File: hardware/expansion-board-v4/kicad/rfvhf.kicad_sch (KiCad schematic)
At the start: 19 parts, among them J10 U.FL_VHF(经尾线转SMA), U21 BK4819QN32SC, U22 PCM1808PWR, Y4 26MHz TCXO <=2.5ppm

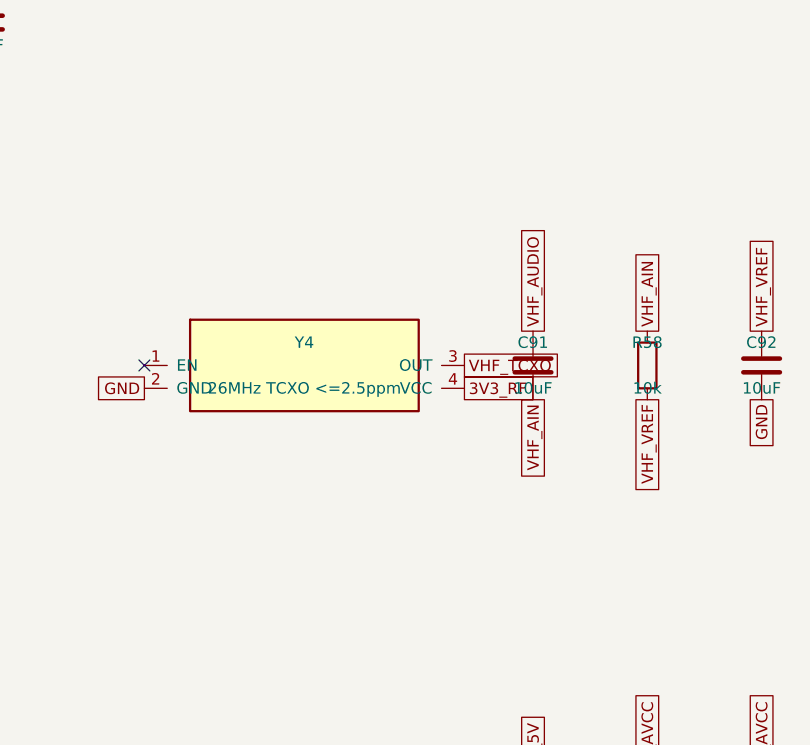
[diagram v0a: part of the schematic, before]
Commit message: v4.7: SW3 主电源键接 /QON + TCXO 输出隔直 + 覆铜填充参数固化
**SW3 主电源键**。电池在位时 SYS 恒供电，整板此前没有任何机械总电门：
微雪 Key3 只关得掉载板自己，而整机 5V 是扩展板升压产的；J1 的 40 脚里
没有一根电源控制线。唯一出路是 SY6970 的 BATFET——所以引 U19.12(/QON)
到板边的 TS24CA 侧按键（按住 1.25~2.25s 开机，BUS 拔掉时按 12~18s 硬复位），
不依赖固件。摆在 USB 口同侧贴板边 (97.882, 39.103)，R7/R8 那组往板内让 4mm 腾位。

封装按规格书 1:1：电气端子 1.2×0.6 中心距 3.4、固定脚 1.3×1.05 外缘跨度 5.3、
两个 φ0.55 定位孔在 X+0.70。两个坑记在封装 descr 里：①定位孔的 layers 必须写
「*.Cu」而不是「F&B.Cu」，否则 6 层板的内层覆铜照样压上来（每孔 5 条
hole_clearance、实际间距 0）；②孔心不能按「上下排焊盘空档的中心」推，那样
错 0.75mm、柱子插不进去。

**TCXO 输出隔直**。Epson brief sheet 的输出负载条件栏写死 DC cut = 0.01µF，
原设计 Y4.3 直连 BK4819 的 XI。补 C99(0402 100pF C0G) 串联 + R61(0402 10k)
负载，VHF_TCXO 拆成 VHF_TCXO_OUT / VHF_TCXO 两网。这里只能用 0402：两焊盘
净空 2.28mm，0603 含焊盘约 2.8mm 放不下，而 Y4 四周被 C76/C98/U21 夹死挪不开。
Y4 符号 pin1 由 EN 改 NC（选型库 fcfYN=N，无压控，悬空正确）。

**覆铜填充参数固化**（本次真正的回归修复）。ZONES.json 此前不含 fill 参数，
重放时 clearance 从板上的 0.15 退回 KiCad 默认 0.5，结果是 2 条网络断开、
4 个悬空端、4 个焊盘未连通——而 DRC 报 0 违例。「DRC 全绿」和「板子是错的」
可以同时成立，因为 zone 的 local clearance 不是 DRC 可见参数。现在导出/回填
clearance、min_thickness、pad_connection、thermal_gap/spoke、island_removal，
并加门禁：任何非 rule-area 的 zone 没拿到固化参数就炸。

装配助手加 v4.7-pwr / v4.7-nopwr，v4.6-* 转归档（元件数据不动，只在副标题
注明「无 SW3 电源键」）。SW3 属于电源区，不带电源版不贴它：207/82 → 180/67。

英文同步器补阶段 G（Airband）并加未登记阶段即炸的护栏：此前中文表加了 G，
而这里只认 A–F，stage 变量保持上一轮的 F 不变，19 个 airband 件被整段并进
「Stage F: External Interface」（1 件变 20 件），两边都不报错、产物看着完整。

Gerber/源包重出为 V4.7-20260913（制造内容与先前那版逐字节相同，仅时间戳行
不同；源包重出是为了让包内 PCB 与工作树一致）。

hardware 契约 80 条：76 通过、4 条 expansion-board-v3 的 RP_1V1 既存豁免不在
本次范围。interface.kicad_sch 工作树里有一份纯 uuid 变更、来源不明，未纳入。
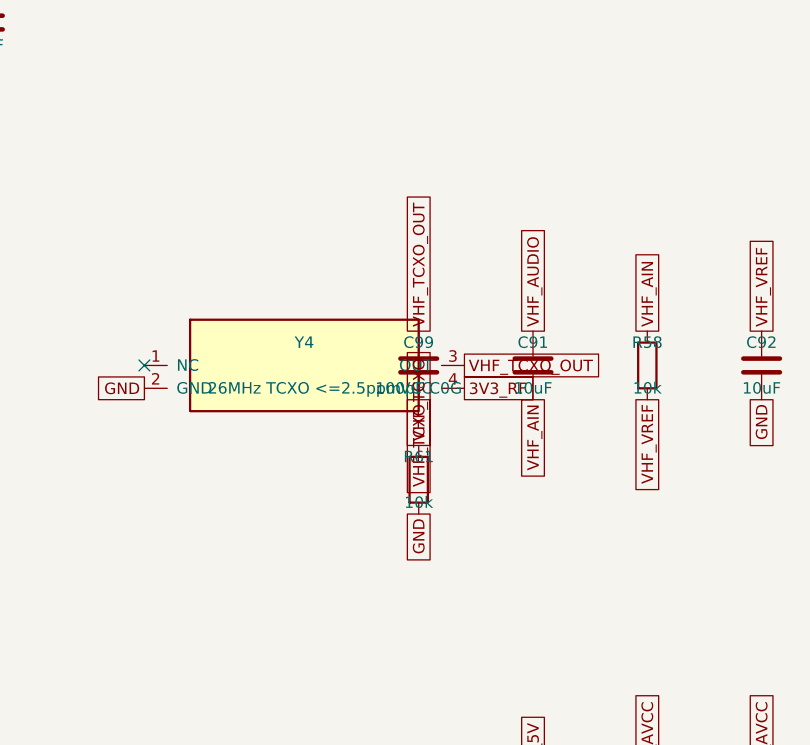
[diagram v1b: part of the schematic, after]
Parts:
- added C99: 100pF C0G, Capacitor_SMD:C_0402_1005Metric, symbol Device:C
- added R61: 10k, Resistor_SMD:R_0402_1005Metric, symbol Device:R
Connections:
- net GND: now also R61.2
- net VHF_TCXO: now also C99.2, R61.1; no longer Y4.3 (OUT)
- new net VHF_TCXO_OUT: C99.1, Y4.3 (OUT)
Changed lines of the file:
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@@
 		(effects (font (size 1.27 1.27)) (justify right))
 	)
-	(global_label "VHF_TCXO"
+	(global_label "VHF_TCXO_OUT"
 		(shape passive)
 		(at 157.48 88.9 0)
@@
 	)
 	(symbol
+		(lib_id "Device:C")
+		(at 152.4 88.9 0)
+		(unit 1)
+		(exclude_from_sim no)
+		(in_bom yes)
+		(on_board yes)
+		(dnp no)
+		(property "Reference" "C99"
+			(at 152.4 86.36 0)
+			(effects (font (size 1.27 1.27)))
+		)
+		(property "Value" "100pF C0G"
+			(at 152.4 91.44 0)
+			(effects (font (size 1.27 1.27)))
+		)
+		(property "Footprint" "Capacitor_SMD:C_0402_1005Metric"
+			(at 152.4 93.98 0)
+			(effects (font (size 1.27 1.27))
+				(hide yes))
+		)
+		(property "Datasheet" "~"
+			(at 152.4 96.52 0)
+			(effects (font (size 1.27 1.27))
+				(hide yes))
+		)
+		(pin "1"
+		)
+		(pin "2"
+		)
+		(instances
+			(project "expansion-board-v4"
+				(path "/10000000-0000-4000-8000-000000000001/20000000-0000-4000-8000-000000000007"
+					(reference "C99")
+					(unit 1)
+				)
+			)
+		)
+	)
+	(global_label "VHF_TCXO_OUT"
+		(shape passive)
+		(at 152.4 85.09 270)
+		(effects (font (size 1.27 1.27)) (justify left))
+	)
+	(global_label "VHF_TCXO"
+		(shape passive)
+		(at 152.4 92.71 90)
+		(effects (font (size 1.27 1.27)) (justify right))
+	)
+	(symbol
+		(lib_id "Device:R")
+		(at 152.4 101.6 0)
+		(unit 1)
+		(exclude_from_sim no)
+		(in_bom yes)
+		(on_board yes)
+		(dnp no)
+		(property "Reference" "R61"
+			(at 152.4 99.06 0)
+			(effects (font (size 1.27 1.27)))
+		)
+		(property "Value" "10k"
+			(at 152.4 104.14 0)
+			(effects (font (size 1.27 1.27)))
+		)
+		(property "Footprint" "Resistor_SMD:R_0402_1005Metric"
+			(at 152.4 106.68 0)
+			(effects (font (size 1.27 1.27))
+				(hide yes))
+		)
+		(property "Datasheet" "~"
+			(at 152.4 109.22 0)
+			(effects (font (size 1.27 1.27))
+				(hide yes))
+		)
+		(pin "1"
+		)
+		(pin "2"
+		)
+		(instances
+			(project "expansion-board-v4"
+				(path "/10000000-0000-4000-8000-000000000001/20000000-0000-4000-8000-000000000007"
+					(reference "R61")
+					(unit 1)
+				)
+			)
+		)
+	)
+	(global_label "VHF_TCXO"
+		(shape passive)
+		(at 152.4 97.79 270)
+		(effects (font (size 1.27 1.27)) (justify left))
+	)
+	(global_label "GND"
+		(shape passive)
+		(at 152.4 105.41 90)
+		(effects (font (size 1.27 1.27)) (justify right))
+	)
+	(symbol

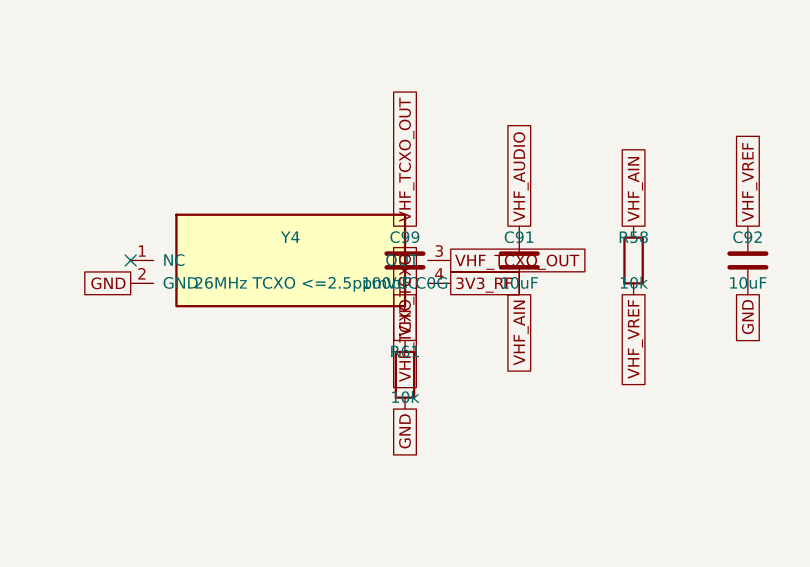
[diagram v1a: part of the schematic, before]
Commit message: hardware(v4.7): 修正 C99 并刷新整套制造与装配文件
在用户修订的布局上将 C99 改为 100nF/0402，复用 C37/C52 的 C307331；同步原理图版本、BOM/CPL、装配图、安装助手及制造归档，更新下单入口和未决电气项。

验证：DRC 0 违规/0 未连通，存盘覆铜与包源一致性已核对；提交前版本包/安装助手20项，18通过、2跳过。元件契约中已记录的 C84 两条子断言失败按用户范围保留；Y4 供电和 U22 VREF 建议尚待闭环。内部工具、审计报告和采购过程文件按仓库规则仅留本地。
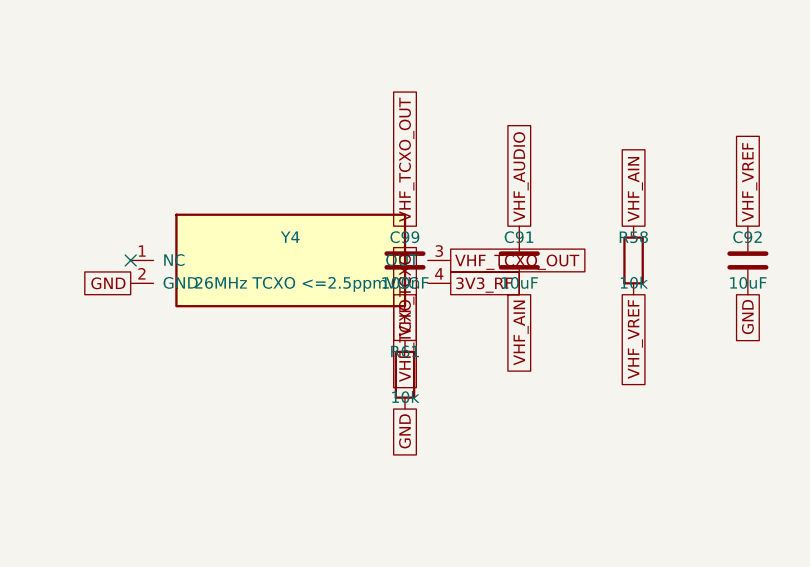
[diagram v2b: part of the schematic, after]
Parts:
- C99: value 100pF C0G -> 100nF
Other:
- title: Expansion Board V4.6 - VHF airband: BK4819 RX + PCM1808 capture -> Expansion Board V4.7 - VHF airband: BK4819 RX + PCM1808 capture
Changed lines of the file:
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@@
 	(paper "A3")
 	(title_block
-		(title "Expansion Board V4.6 - VHF airband: BK4819 RX + PCM1808 capture")
+		(title "Expansion Board V4.7 - VHF airband: BK4819 RX + PCM1808 capture")
 		(date "2026-08-01")
-		(rev "V1")
+		(rev "V4.7")
 		(company "Pilot Kit")
 	)
@@
 			(effects (font (size 1.27 1.27)))
 		)
-		(property "Value" "100pF C0G"
+		(property "Value" "100nF"
 			(at 152.4 91.44 0)
 			(effects (font (size 1.27 1.27)))

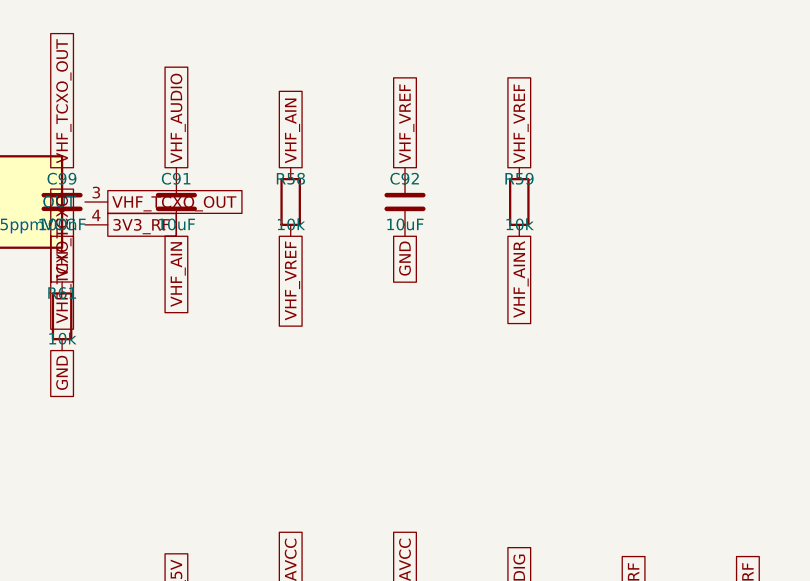
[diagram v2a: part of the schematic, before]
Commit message: hardware(v4.7): VHF VREF 去耦定稿为 C100，全链路刷新
本次提交合并了两路并行工作，V4.7 至此定稿。

一、并行 session 的 VHF 收尾（不是我做的）
   给 VHF_VREF 补一颗 100nF 去耦，原位号 C102；同时刷新了装配文档、
   CHECKLIST、发布包与 release/archive 备份。

二、位号改为 C100（本次）
   原位号 C102 跳过了 C100/C101——那两个曾被另一路「GNSS VBAT 常供电」
   方案短暂占用过。该方案已整体移出 V4.7、改到 V4.8 做，于是这里空出两个
   号。位号紧接 C99 收敛成 C100，批次干净，不留空洞。

   改名波及六处，逐处核过：
     · sheet_rfvhf.py（原理图源）
     · kicad_pcb 的 Reference 属性（只改这一处，不碰网络与几何）
     · PLACEMENT.py 两条：元件位 + 丝印位
     · ROUTES.json / SILK.json —— 0 处，本来就不引位号
     · ASSEMBLY / CHECKLIST / BOM / README / 内部文档
     · release/smt 六个 CSV + Gerber 与源码包

   两个坑值得记下来：
   1) SMT 产物有三个变体（minimal / passives / full），gen_jlc_smt.py 默认
      只出 passives。只跑默认那次，full 和 minimal 里的 C102 原样留着，而
      它们正是要上传给嘉立创的那两份。
   2) 正则 \bC102\b 在中文语境下不成立——中文字符也算 \w，"及C102" 中间
      没有词边界，于是「及C102」「C99/R61及C102」「C102已完成」三处静默漏掉。
      改用先断言无 C102x 再直接替换。

   另：kicad/ 下的评审 PDF 是 19:10 出的，早于改名，里面还印着 C102 —— 已
   重新导出并核对为 C100。check_docs_sync.py 只比对标题版本、不看内容，
   这类过时它抓不到。板目录根部另有一份同源重复的 PDF，已移出。

验收
   布局契约门禁 13 项全绿
   DRC：铜层 0 违例 / 丝印 0 违例 / 未连通 0 / In1 参考面完整
   文档坐标核对 416 处、0 处对不上；标题版本 0 份不符
   新旧发布包丝印层比对：差异 64 行，量级与「一个位号改一个字符」吻合

⚠️ check_gerber.py 没跑——它依赖 gerbonara，本机未安装，我没擅自 pip install。
   上面的丝印层比对是替代判据，**不覆盖**它对 274X 格式与原点参数的检查。
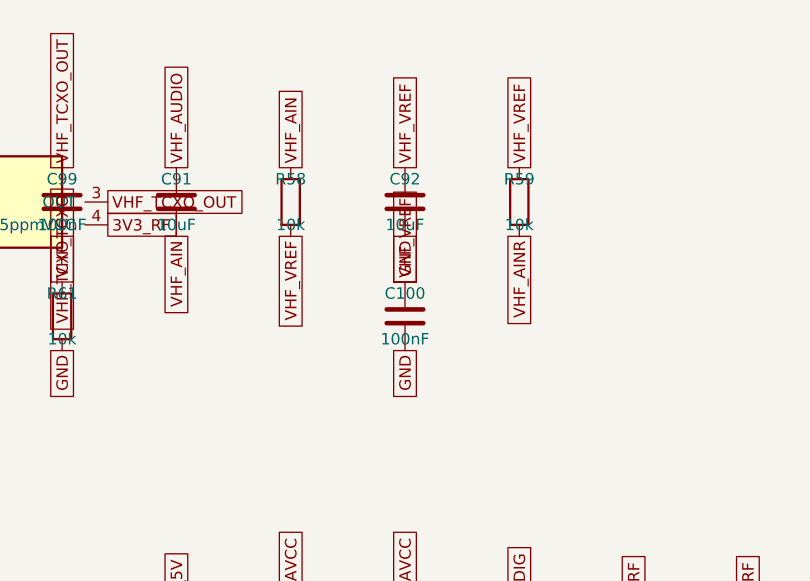
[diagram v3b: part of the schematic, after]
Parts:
- added C100: 100nF, Capacitor_SMD:C_0603_1608Metric, symbol Device:C
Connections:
- net GND: now also C100.2
- net VHF_VREF: now also C100.1
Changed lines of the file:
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@@
+	)
+	(symbol
+		(lib_id "Device:C")
+		(at 190.5 101.6 0)
+		(unit 1)
+		(exclude_from_sim no)
+		(in_bom yes)
+		(on_board yes)
+		(dnp no)
+		(property "Reference" "C100"
+			(at 190.5 99.06 0)
+			(effects (font (size 1.27 1.27)))
+		)
+		(property "Value" "100nF"
+			(at 190.5 104.14 0)
+			(effects (font (size 1.27 1.27)))
+		)
+		(property "Footprint" "Capacitor_SMD:C_0603_1608Metric"
+			(at 190.5 106.68 0)
+			(effects (font (size 1.27 1.27))
+				(hide yes))
+		)
+		(property "Datasheet" "~"
+			(at 190.5 109.22 0)
+			(effects (font (size 1.27 1.27))
+				(hide yes))
+		)
+		(pin "1"
+		)
+		(pin "2"
+		)
+		(instances
+			(project "expansion-board-v4"
+				(path "/10000000-0000-4000-8000-000000000001/20000000-0000-4000-8000-000000000007"
+					(reference "C100")
+					(unit 1)
+				)
+			)
+		)
+	)
+	(global_label "VHF_VREF"
+		(shape passive)
+		(at 190.5 97.79 270)
+		(effects (font (size 1.27 1.27)) (justify left))
+	)
+	(global_label "GND"
+		(shape passive)
+		(at 190.5 105.41 90)
+		(effects (font (size 1.27 1.27)) (justify right))
 	)
 	(symbol

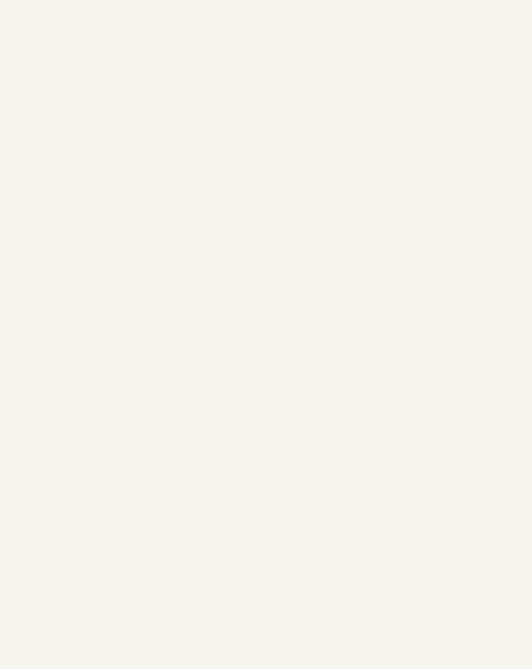
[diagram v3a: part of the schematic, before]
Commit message: hardware(v4.10): J11 改 2x10 测试焊盘阵列并入 airband；26MHz 探测点加隔离电阻 R66
J11 由 V4.9 的 2x8 贴片排针改成 2x10 裸焊盘阵列（自制封装
TestPad_2x10_P2.54mm：20 个 φ1.0mm 裸铜、2.54 网格、不贴任何件），
配 2x10p PCB 测试夹。中心上移 2.54mm，让新 pin5~20 精确落在原 pin1~16
的物理位置，16 根已布走线一根未动；但两列中心距从排针的 5.05mm 收到
探针的 2.54mm，20 个焊盘各内收 1.26mm，走线端点随之跟进。

两处会让人照旧图读错板的改动：
- 脚号整体后移 4 位，且跳线帽消失、三对短接改用镊子/锡桥
  （复位 1-2→5-6、BOOTSEL 3-4→7-8、自检回环 15-16→19-20）。
- 焊盘定 φ1.0 而不是 φ1.2：两列之间要并排走 4 根 0.15mm 线，
  按 0.15 间距需 1.35mm 净宽，φ1.2 只剩 1.34mm，差 0.01mm 塞不下。

新增 airband 四脚（VHF_TCXO_TP / VHF_AUDIO / VHF_SCK / VHF_SDATA），
沿板子下缘布通，在 1090 接收前端所在的 y 50.5~58 带内铜长 0.0mm。
26MHz 参考经 R66（0Ω 0603，**默认不贴**）隔离：那根分支 119.9mm 走 In2，
直连会给 TG-5006CG 加约 17pF，而手册 Output load 是 10kΩ // 10pF、
fo-Load 条件栏写死 ±10%。频率不是主要风险，幅度才是——0.8Vpp Min 是在
10pF 下保证的，27pF 在 26MHz 只剩 227Ω，而 BK4819 的 XI 是并联谐振晶体口、
手册没给外部注入门限，参考起不来就是 airband 整条收不了。
R66 必须在 TCXO 端；放 J11 端那 120mm 仍挂在振荡节点上，等于白做。
不贴时振荡节点残留 11.0mm + 2 过孔 ≈ 1.8pF。

丝印：B 面 20 格图例 + J11 旁竖排行号（偶数脚 2~20，与焊盘行逐行对齐，
离本体 1.0mm）。图例与 J11 位号的最终位置由维护者手工定稿后固化，
独立的 "J11" 板级文字因与位号重复已删除。

顺带修掉四处会静默出错的地方：
- gen_j11_silk 的障碍模型错了三次：B.SilkS 层名比对恒假（避让从未生效）、
  改宽后把 F 面丝印和 F 面贴片焊盘也当成 B 面丝印的障碍（误判"放不下"）。
  已按"只算 B 面"收敛，并加防覆盖闸：板上已有整套图例时拒绝重排。
- SHORT 漏缩写会让单元格回退成完整网名，那串既不匹配 drop 的正则、
  又撑爆表格布局，在板上越积越多；已加覆盖断言。
- R66 的「默认不贴」要在五份名单里登记，gen_master_bom 的护栏当场抓到漏项。
- 合同补上行号列与图例的位置断言，不只查文字存在。

验证：DRC 0 违例 / 0 未连通 / 丝印 0 违例；文档坐标 438 处 0 处对不上；
硬件合同 73 passed / 8 skipped。check_gerber 的 ⑤ 项与历史包逐字相同，
是本板恒报的 SW3 机械固定脚，非本轮引入。

发布包：V4.8 移出 release/（留档 build/v48-superseded/），
V4.9 按已下单存入 release/archive/20260915-V4.9-ordered/，
当前可下单为 V4.10-20260921。
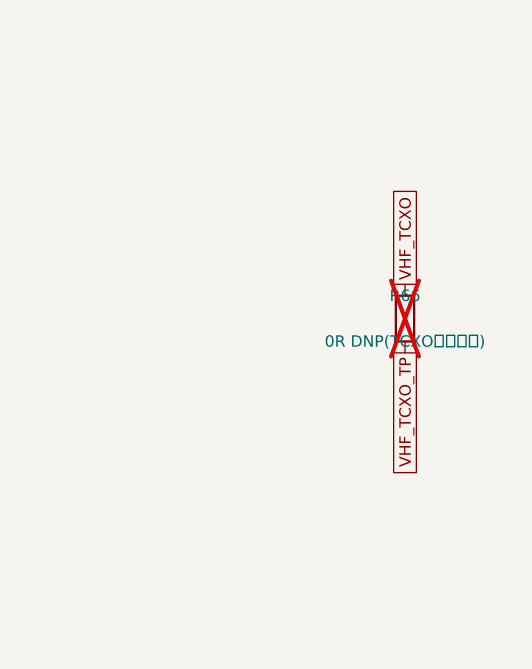
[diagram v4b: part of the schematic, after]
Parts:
- added R66: 0R DNP(TCXO探测隔离), Resistor_SMD:R_0603_1608Metric, symbol Device:R
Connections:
- net VHF_TCXO: now also R66.1
- new net VHF_TCXO_TP: R66.2
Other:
- title: Expansion Board V4.7 - VHF airband: BK4819 RX + PCM1808 capture -> Expansion Board V4.10 - VHF airband: BK4819 RX + PCM1808 capture
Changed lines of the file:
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@@
 	(paper "A3")
 	(title_block
-		(title "Expansion Board V4.7 - VHF airband: BK4819 RX + PCM1808 capture")
+		(title "Expansion Board V4.10 - VHF airband: BK4819 RX + PCM1808 capture")
 		(date "2026-08-01")
-		(rev "V4.7")
+		(rev "V4.10")
 		(company "Pilot Kit")
 	)
@@
 		(effects (font (size 1.27 1.27)) (justify right))
 	)
+	(symbol
+		(lib_id "Device:R")
+		(at 254 88.9 0)
+		(unit 1)
+		(exclude_from_sim no)
+		(in_bom yes)
+		(on_board yes)
+		(dnp yes)
+		(property "Reference" "R66"
+			(at 254 86.36 0)
+			(effects (font (size 1.27 1.27)))
+		)
+		(property "Value" "0R DNP(TCXO探测隔离)"
+			(at 254 91.44 0)
+			(effects (font (size 1.27 1.27)))
+		)
+		(property "Footprint" "Resistor_SMD:R_0603_1608Metric"
+			(at 254 93.98 0)
+			(effects (font (size 1.27 1.27))
+				(hide yes))
+		)
+		(property "Datasheet" "~"
+			(at 254 96.52 0)
+			(effects (font (size 1.27 1.27))
+				(hide yes))
+		)
+		(pin "1"
+		)
+		(pin "2"
+		)
+		(instances
+			(project "expansion-board-v4"
+				(path "/10000000-0000-4000-8000-000000000001/20000000-0000-4000-8000-000000000007"
+					(reference "R66")
+					(unit 1)
+				)
+			)
+		)
+	)
+	(global_label "VHF_TCXO"
+		(shape passive)
+		(at 254 85.09 270)
+		(effects (font (size 1.27 1.27)) (justify left))
+	)
+	(global_label "VHF_TCXO_TP"
+		(shape passive)
+		(at 254 92.71 90)
+		(effects (font (size 1.27 1.27)) (justify right))
+	)

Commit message: feat(v4.11): 固化扩展板并修正电池补偿
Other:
- title: Expansion Board V4.10 - VHF airband: BK4819 RX + PCM1808 capture -> Expansion Board V4.11 - VHF airband: BK4819 RX + PCM1808 capture
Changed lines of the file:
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@@
 	(paper "A3")
 	(title_block
-		(title "Expansion Board V4.10 - VHF airband: BK4819 RX + PCM1808 capture")
+		(title "Expansion Board V4.11 - VHF airband: BK4819 RX + PCM1808 capture")
 		(date "2026-08-01")
-		(rev "V4.10")
+		(rev "V4.11")
 		(company "Pilot Kit")
 	)
